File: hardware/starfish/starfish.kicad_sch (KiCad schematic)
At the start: 4 parts

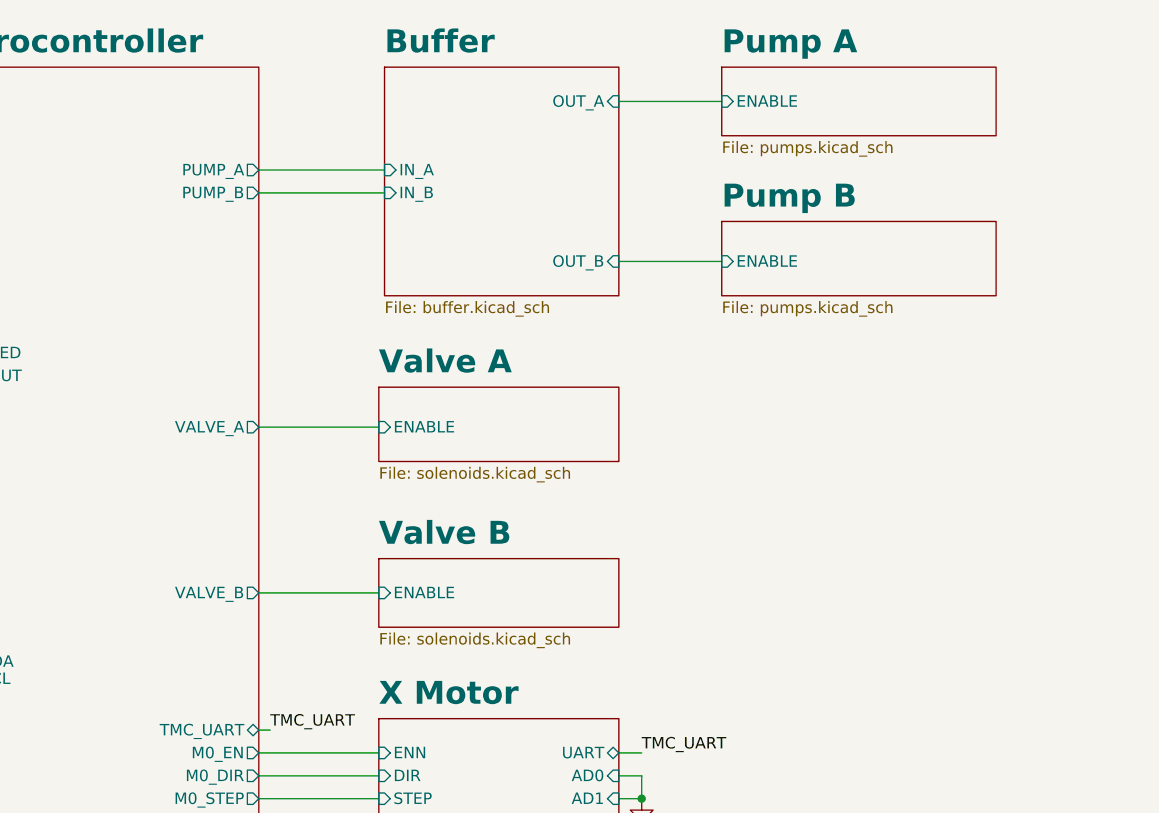
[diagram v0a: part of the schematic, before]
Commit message: Starfish v1
- Switch from DRV120 smart solenoid drivers to MOSFETs so that a wider variety of solenoids can be controlled. RP2040 PWM should be used along with these MOSFETs to prevent solenoids from overheating.
- Move all power lines out of inner copper layers and onto back copper.
- Small changes to signal routing to accommodate new power routing.
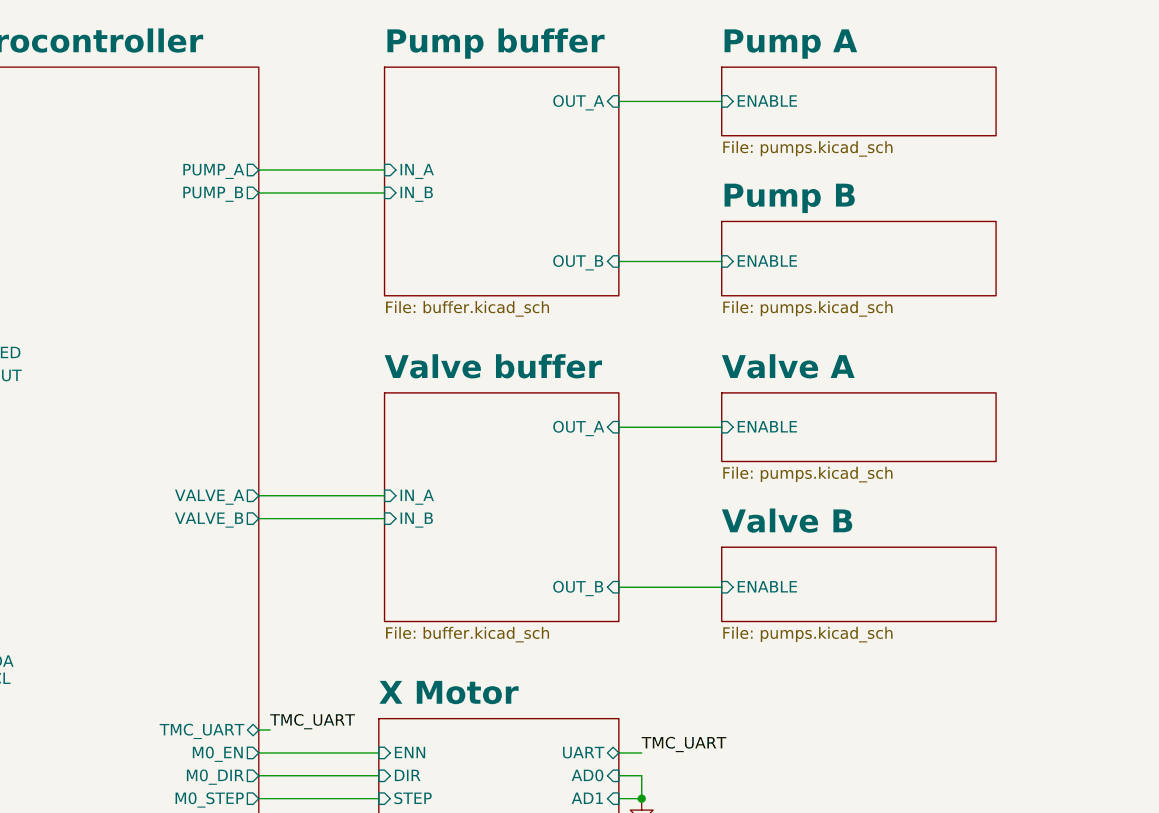
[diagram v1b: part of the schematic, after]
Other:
- sheet Buffer renamed Pump buffer
- added sheet Valve buffer (buffer.kicad_sch)
- sheet Valve A: file solenoids.kicad_sch -> pumps.kicad_sch
- sheet Valve B: file solenoids.kicad_sch -> pumps.kicad_sch
